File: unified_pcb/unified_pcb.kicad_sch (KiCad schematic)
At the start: 97 parts, among them J1 Conn_01x02_Socket, J2 USB_C_Receptacle, J3 Conn_01x02_Socket, J4 Conn_01x03_Pin, Q1 Q_Photo_NPN, Q2 Q_Photo_NPN, Q3 Q_Photo_NPN, SW1 SW_Push, SW2 SW_Push, U1 BQ27427YZFR, U10 3.3V LDO, U11 LMD4030T261-OA1, U12 LY4176D, U13 MMC5603NJ, U14 BMI270, U2 USBLC6-2P6, U3 3.3V LDO, U4 RP2350_60QFN, U7 QSPI Flash, U8 TPGLF72101CSP4, Y1 12MHz

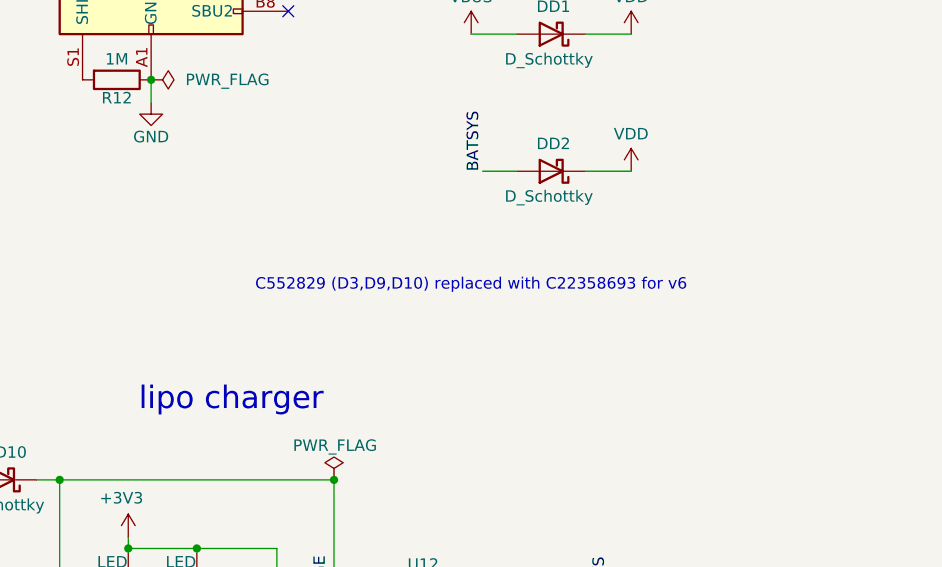
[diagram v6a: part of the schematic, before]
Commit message: note about part replacement on v7 order
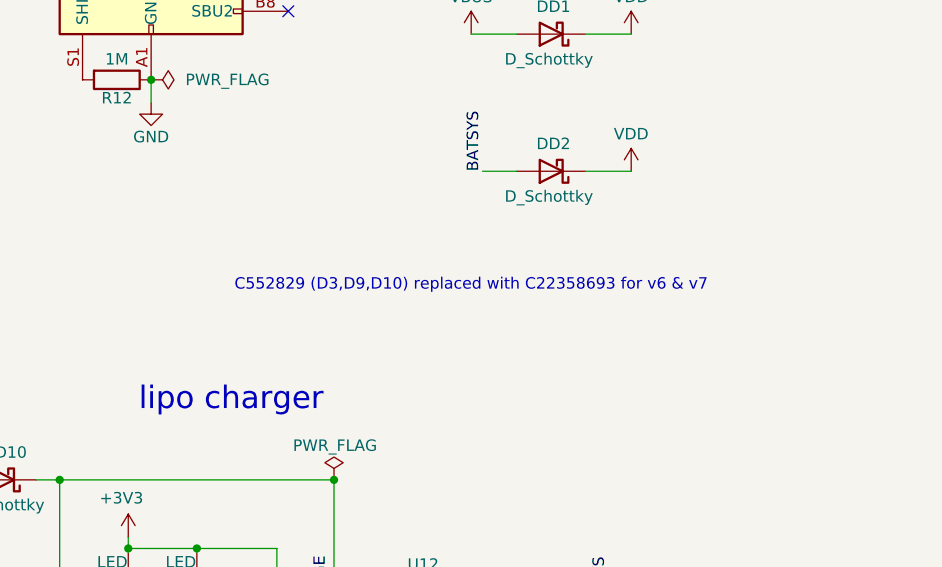
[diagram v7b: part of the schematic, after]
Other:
- note added: "C552829 (D3,D9,D10) replaced with C22358693 for v6 & v7"
- note removed: "C552829 (D3,D9,D10) replaced with C22358693 for v6"
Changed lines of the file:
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@@
 		)
 	)
-	(text "C552829 (D3,D9,D10) replaced with C22358693 for v6"
+	(text "C552829 (D3,D9,D10) replaced with C22358693 for v6 & v7"
 		(exclude_from_sim no)
 		(at 76.2 132.08 0)

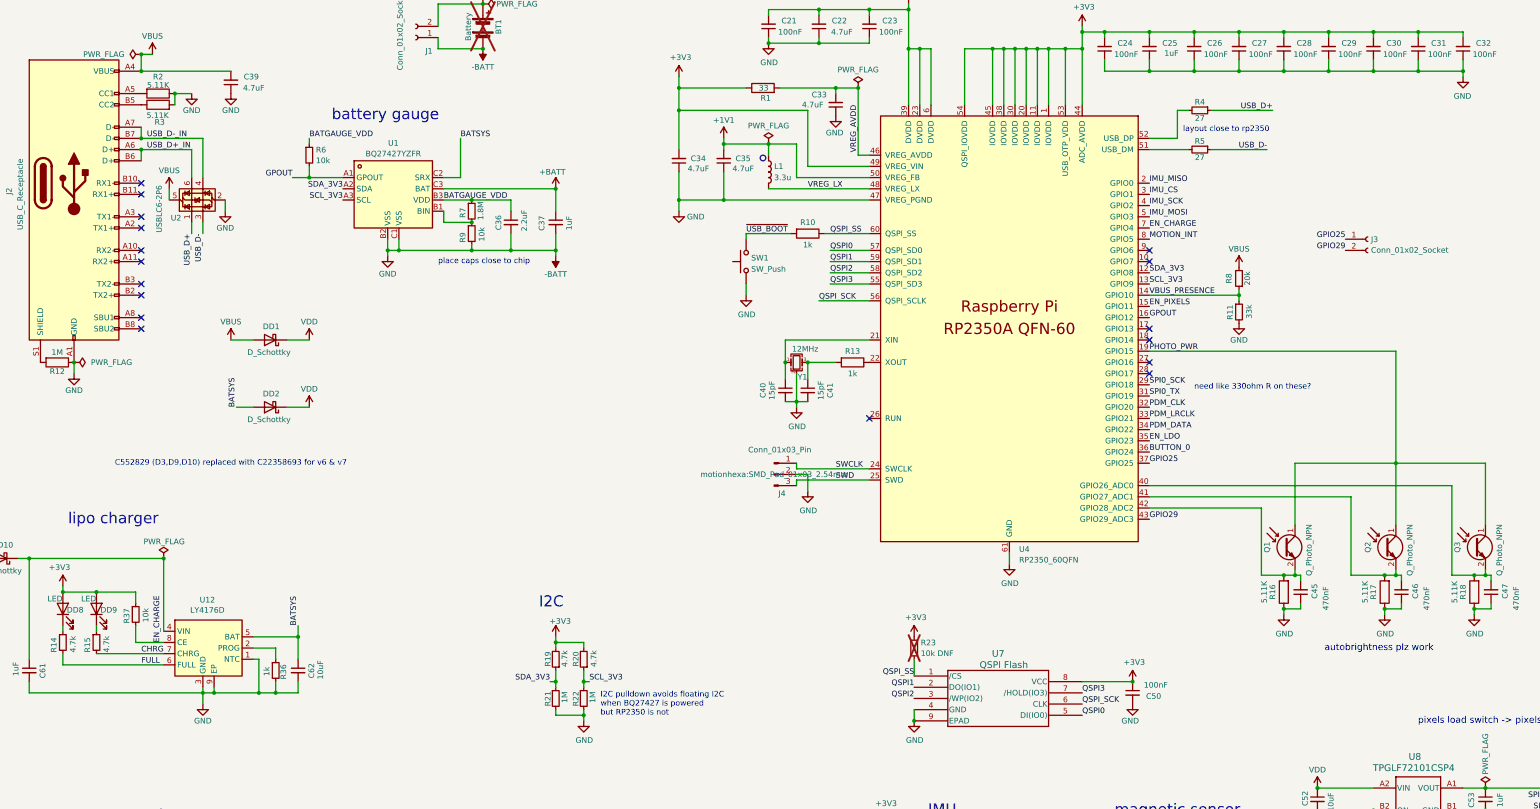
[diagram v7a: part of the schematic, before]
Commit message: batsys ->| vbus gets a mosfet for battery efficiency; switch from rp2350 to rp2354 since qspi memory chip is low stock and this is cheaper anyway; bom replacements for diodes and passives for out of stock and cost improvements;
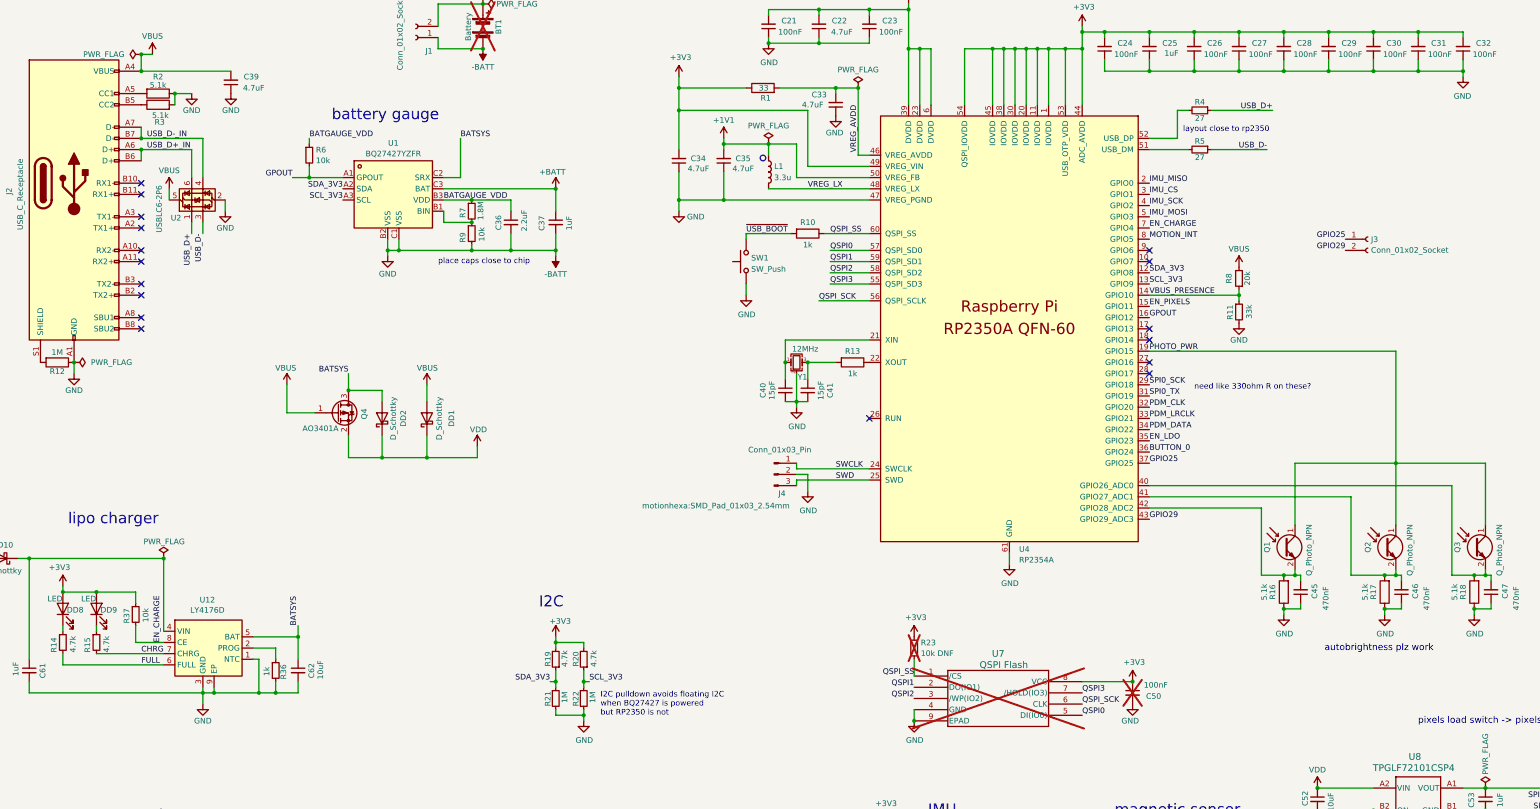
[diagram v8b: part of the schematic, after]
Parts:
- added Q4: AO3401A, Package_TO_SOT_SMD:SOT-23, symbol Transistor_FET:AO3401A
- C21, C23, C24, C26, C27, C28, C29, C30, C31, C32, C60, C64, C65: Designation CC0402KRX7R7BB104 -> CL05B104KO5NNNC; LCSC C60474 -> C1525
- C22, C33, C34, C35, C39: Designation CL05A475KP5NRNC -> CL05A475MP5NRNC; LCSC C368809 -> C23733
- C25, C37, C38, C48, C53, C58, C59, C61: Designation CL05A105KP5NNNC -> CL05A105KA5NQNC; LCSC C14445 -> C52923
- C50: Designation CC0402KRX7R7BB104 -> CL05B104KO5NNNC; LCSC C60474 -> C1525; now not fitted; now left out of the parts list
- C52, C62: Designation 0603X106K100 -> CL10A106KP8NNNC; LCSC C90806 -> C19702
- DD1, DD10, DD2: Designation PMEG2010EPK,315 -> TPMEG4020EPK; LCSC C552829 -> C22358693
- DD6, DD7: Designation PMEG4002EL,315 -> RB521BS-30-MS; LCSC C426866 -> C2847014
- R10, R13, R24, R36: Designation RC0402FR-071KL -> 0402WGF1001TCE; LCSC C106235 -> C11702
- R12, R21, R22: Designation RC0402JR-071ML -> 0402WGF1004TCE; LCSC C93949 -> C26083
- R14, R15, R19, R20, R32: Designation FRC0402J472 TS -> 0402WGF4701TCE; LCSC C2906941 -> C25900
- R16, R17, R18, R2, R3: value 5.11K -> 5.1k; Designation RC0402FR-075K11L -> 0402WGF5101TCE; LCSC C274895 -> C25905
- R31, R37, R6, R9: Designation RC0402FR-0710KL -> 0402WGF1002TCE; LCSC C60490 -> C25744
- R33, R8: Designation RC0402FR-0720KL -> 0402WGF2002TCE; LCSC C93942 -> C25765
- SW1: Designation (none) -> HX-B3U-1000P-1.6N; LCSC C2905190 -> C49234121
- U4: value RP2350_60QFN -> RP2354A; Designation (none) -> RP2354A; LCSC C42411118 -> C41378174
- U7: now not fitted; now left out of the parts list
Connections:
- net BATSYS: now also Q4.3 (D)
- net VBUS: now also Q4.1 (G)
- net VDD: now also Q4.2 (S)
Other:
- note removed: "C552829 (D3,D9,D10) replaced with C22358693 for v6 & v7"
- moved on the sheet: DD1
